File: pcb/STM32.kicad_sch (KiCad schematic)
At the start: 17 parts, among them J2 TC2030, J3 Conn_02x08_Top_Bottom, SW1 SW_Push, SW2 SW_Push, U3 STM32F103C8T6, Y1 8MHz

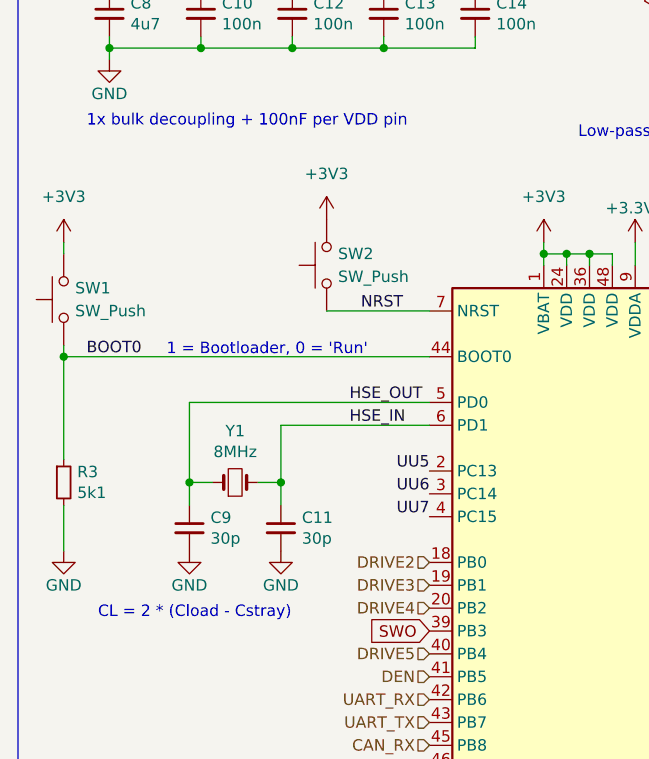
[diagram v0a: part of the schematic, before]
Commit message: Started layout
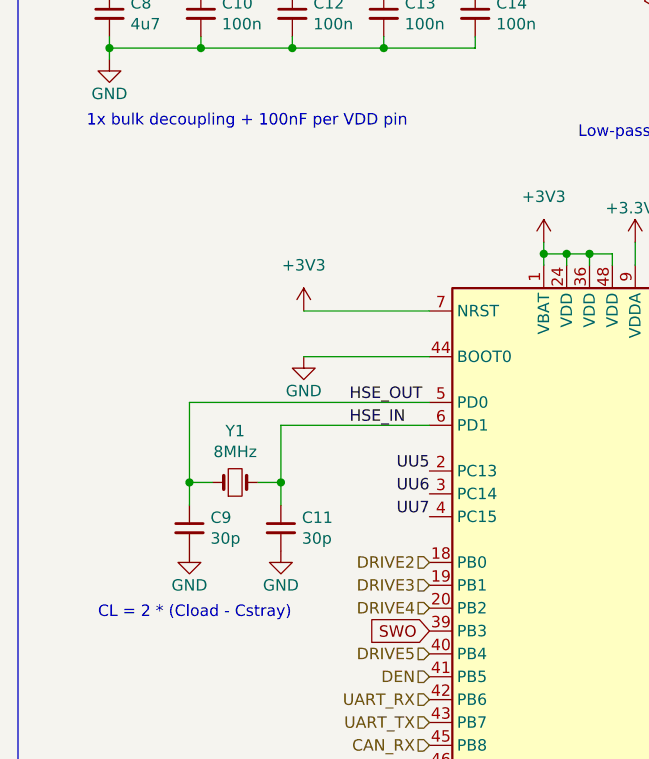
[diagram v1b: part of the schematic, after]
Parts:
- removed R3: 5k1, Resistor_SMD:R_0603_1608Metric, symbol Device:R_Small
- removed SW1, SW2: SW_Push, Button_Switch_SMD:SW_Push_1P1T_NO_CK_KSC7xxJ, symbol Switch:SW_Push
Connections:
- net BOOT0 is gone; now on net GND: U3.44 (BOOT0)
- net NRST is gone; now on net +3V3: U3.7 (NRST)
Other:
- note removed: "1 = Bootloader, 0 = 'Run'"
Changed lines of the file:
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@@
   (junction (at 77.47 52.07) (diameter 0) (color 0 0 0 0)
-  )
-  (junction (at 62.23 93.98) (diameter 0) (color 0 0 0 0)
   )
   (junction (at 87.63 59.69) (diameter 0) (color 0 0 0 0)
@@
     (stroke (width 0) (type default) (color 0 0 0 0))
   )
-  (wire (pts (xy 91.44 88.9) (xy 102.87 88.9))
-    (stroke (width 0) (type default) (color 0 0 0 0))
-  )
   (wire (pts (xy 115.57 162.56) (xy 115.57 161.29))
     (stroke (width 0) (type default) (color 0 0 0 0))
@@
     (stroke (width 0) (type default) (color 0 0 0 0))
   )
-  (wire (pts (xy 102.87 93.98) (xy 62.23 93.98))
-    (stroke (width 0) (type default) (color 0 0 0 0))
-  )
   (wire (pts (xy 134.62 62.23) (xy 134.62 60.96))
     (stroke (width 0) (type default) (color 0 0 0 0))
@@
     (stroke (width 0) (type default) (color 0 0 0 0))
   )
-  (wire (pts (xy 62.23 93.98) (xy 62.23 105.41))
-    (stroke (width 0) (type default) (color 0 0 0 0))
-  )
   (wire (pts (xy 143.51 53.34) (xy 134.62 53.34))
     (stroke (width 0) (type default) (color 0 0 0 0))
@@
     (stroke (width 0) (type default) (color 0 0 0 0))
   )
-  (wire (pts (xy 62.23 81.28) (xy 62.23 82.55))
-    (stroke (width 0) (type default) (color 0 0 0 0))
-  )
   (wire (pts (xy 134.62 59.69) (xy 134.62 60.96))
     (stroke (width 0) (type default) (color 0 0 0 0))
   )
-  (wire (pts (xy 62.23 115.57) (xy 62.23 110.49))
-    (stroke (width 0) (type default) (color 0 0 0 0))
-  )
   (polyline (pts (xy 57.15 170.18) (xy 166.37 170.18))
     (stroke (width 0) (type default) (color 0 0 0 0))
@@
     (stroke (width 0) (type default) (color 0 0 0 0))
   )
+  (wire (pts (xy 88.9 88.9) (xy 102.87 88.9))
+    (stroke (width 0) (type default) (color 0 0 0 0))
+  )
   (wire (pts (xy 86.36 110.49) (xy 86.36 107.95))
     (stroke (width 0) (type default) (color 0 0 0 0))
@@
     (stroke (width 0) (type default) (color 0 0 0 0))
   )
-  (wire (pts (xy 62.23 92.71) (xy 62.23 93.98))
+  (wire (pts (xy 88.9 93.98) (xy 102.87 93.98))
     (stroke (width 0) (type default) (color 0 0 0 0))
   )
@@
     (effects (font (size 2.0066 2.0066) (thickness 0.4013) bold) (justify left bottom))
   )
-  (text "1 = Bootloader, 0 = 'Run'" (at 73.66 93.98 0)
-    (effects (font (size 1.27 1.27)) (justify left bottom))
-  )
   (text "Programming/debug header.\nPlace in an accessible location close to the mcu."
     (at 181.61 105.41 0)
@@
     (effects (font (size 1.27 1.27)) (justify right bottom))
   )
-  (label "NRST" (at 95.25 88.9 0)
-    (effects (font (size 1.27 1.27)) (justify left bottom))
-  )
   (label "UU3" (at 95.25 152.4 180)
     (effects (font (size 1.27 1.27)) (justify right bottom))
@@
   (label "UU2" (at 95.25 149.86 180)
     (effects (font (size 1.27 1.27)) (justify right bottom))
-  )
-  (label "BOOT0" (at 64.77 93.98 0)
-    (effects (font (size 1.27 1.27)) (justify left bottom))
   )
   (label "UU1" (at 193.04 130.81 180)
@@
     (pin "1")
   )
-  (symbol (lib_id "Device:R_Small") (at 62.23 107.95 0) (unit 1)
-    (in_bom yes) (on_board yes)
-    (property "Reference" "R3" (id 0) (at 63.7286 106.7816 0)
-      (effects (font (size 1.27 1.27)) (justify left))
-    )
-    (property "Value" "5k1" (id 1) (at 63.7286 109.093 0)
-      (effects (font (size 1.27 1.27)) (justify left))
-    )
-    (property "Footprint" "Resistor_SMD:R_0603_1608Metric" (id 2) (at 62.23 107.95 0)
-      (effects (font (size 1.27 1.27)) hide)
-    )
-    (property "Datasheet" "~" (id 3) (at 62.23 107.95 0)
-      (effects (font (size 1.27 1.27)) hide)
-    )
-    (property "LCSC" "C25905" (id 5) (at 62.23 107.95 0)
-      (effects (font (size 1.27 1.27)) hide)
-    )
-    (pin "1")
-    (pin "2")
-  )
-  (symbol (lib_id "Switch:SW_Push") (at 62.23 87.63 90) (unit 1)
+  (symbol (lib_id "power:+3V3") (at 88.9 88.9 0) (unit 1)
     (in_bom yes) (on_board yes) (fields_autoplaced)
-    (property "Reference" "SW1" (id 0) (at 63.5 86.3599 90)
-      (effects (font (size 1.27 1.27)) (justify right))
-    )
-    (property "Value" "SW_Push" (id 1) (at 63.5 88.8999 90)
-      (effects (font (size 1.27 1.27)) (justify right))
-    )
-    (property "Footprint" "Button_Switch_SMD:SW_Push_1P1T_NO_CK_KSC7xxJ" (id 2) (at 57.15 87.63 0)
-      (effects (font (size 1.27 1.27)) hide)
-    )
-    (property "Datasheet" "~" (id 3) (at 57.15 87.63 0)
-      (effects (font (size 1.27 1.27)) hide)
-    )
-    (property "LCSC" "C318884" (id 5) (at 62.23 87.63 0)
-      (effects (font (size 1.27 1.27)) hide)
-    )
-    (pin "1")
-    (pin "2")
+    (property "Reference" "#PWR?" (id 0) (at 88.9 92.71 0)
+      (effects (font (size 1.27 1.27)) hide)
+    )
+    (property "Value" "+3V3" (id 1) (at 88.9 83.82 0))
+    (property "Footprint" "" (id 2) (at 88.9 88.9 0)
+      (effects (font (size 1.27 1.27)) hide)
+    )
+    (property "Datasheet" "" (id 3) (at 88.9 88.9 0)
+      (effects (font (size 1.27 1.27)) hide)
+    )
+    (pin "1")
   )
   (symbol (lib_id "MCU_ST_STM32F1:STM32F103C8Tx") (at 120.65 121.92 0) (unit 1)
@@
     (pin "2")
   )
-  (symbol (lib_id "Switch:SW_Push") (at 91.44 83.82 90) (unit 1)
-    (in_bom yes) (on_board yes) (fields_autoplaced)
-    (property "Reference" "SW2" (id 0) (at 92.71 82.5499 90)
-      (effects (font (size 1.27 1.27)) (justify right))
-    )
-    (property "Value" "SW_Push" (id 1) (at 92.71 85.0899 90)
-      (effects (font (size 1.27 1.27)) (justify right))
-    )
-    (property "Footprint" "Button_Switch_SMD:SW_Push_1P1T_NO_CK_KSC7xxJ" (id 2) (at 86.36 83.82 0)
-      (effects (font (size 1.27 1.27)) hide)
-    )
-    (property "Datasheet" "~" (id 3) (at 86.36 83.82 0)
-      (effects (font (size 1.27 1.27)) hide)
-    )
-    (property "LCSC" "C318884" (id 5) (at 91.44 83.82 0)
-      (effects (font (size 1.27 1.27)) hide)
-    )
-    (pin "1")
-    (pin "2")
-  )
   (symbol (lib_id "power:GND") (at 185.42 95.25 0) (unit 1)
     (in_bom yes) (on_board yes)
@@
     (pin "6")
   )
-  (symbol (lib_id "power:+3V3") (at 62.23 81.28 0) (unit 1)
-    (in_bom yes) (on_board yes) (fields_autoplaced)
-    (property "Reference" "#PWR011" (id 0) (at 62.23 85.09 0)
-      (effects (font (size 1.27 1.27)) hide)
-    )
-    (property "Value" "+3V3" (id 1) (at 62.23 76.2 0))
-    (property "Footprint" "" (id 2) (at 62.23 81.28 0)
-      (effects (font (size 1.27 1.27)) hide)
-    )
-    (property "Datasheet" "" (id 3) (at 62.23 81.28 0)
-      (effects (font (size 1.27 1.27)) hide)
-    )
-    (pin "1")
-  )
-  (symbol (lib_id "power:+3V3") (at 91.44 78.74 0) (unit 1)
-    (in_bom yes) (on_board yes) (fields_autoplaced)
-    (property "Reference" "#PWR017" (id 0) (at 91.44 82.55 0)
-      (effects (font (size 1.27 1.27)) hide)
-    )
-    (property "Value" "+3V3" (id 1) (at 91.44 73.66 0))
-    (property "Footprint" "" (id 2) (at 91.44 78.74 0)
-      (effects (font (size 1.27 1.27)) hide)
-    )
-    (property "Datasheet" "" (id 3) (at 91.44 78.74 0)
-      (effects (font (size 1.27 1.27)) hide)
-    )
-    (pin "1")
-  )
   (symbol (lib_id "Device:C_Small") (at 143.51 57.15 0) (unit 1)
     (in_bom yes) (on_board yes)
@@
     (pin "1")
   )
-  (symbol (lib_id "power:GND") (at 62.23 115.57 0) (unit 1)
-    (in_bom yes) (on_board yes)
-    (property "Reference" "#PWR012" (id 0) (at 62.23 121.92 0)
-      (effects (font (size 1.27 1.27)) hide)
-    )
-    (property "Value" "GND" (id 1) (at 62.23 119.38 0))
-    (property "Footprint" "" (id 2) (at 62.23 115.57 0)
-      (effects (font (size 1.27 1.27)) hide)
-    )
-    (property "Datasheet" "" (id 3) (at 62.23 115.57 0)
-      (effects (font (size 1.27 1.27)) hide)
-    )
+  (symbol (lib_id "power:GND") (at 88.9 93.98 0) (unit 1)
+    (in_bom yes) (on_board yes)
+    (property "Reference" "#PWR012" (id 0) (at 88.9 100.33 0)
+      (effects (font (size 1.27 1.27)) hide)
+    )
+    (property "Value" "GND" (id 1) (at 88.9 97.79 0))
+    (property "Footprint" "" (id 2) (at 88.9 93.98 0)
+      (effects (font (size 1.27 1.27)) hide)
+    )
+    (property "Datasheet" "" (id 3) (at 88.9 93.98 0)
+      (effects (font (size 1.27 1.27)) hide)
+    )

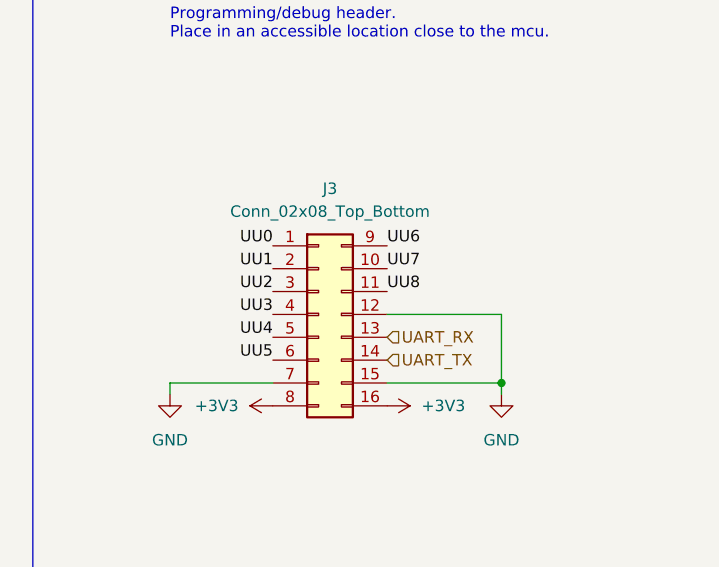
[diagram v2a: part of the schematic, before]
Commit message: Fixed ERC
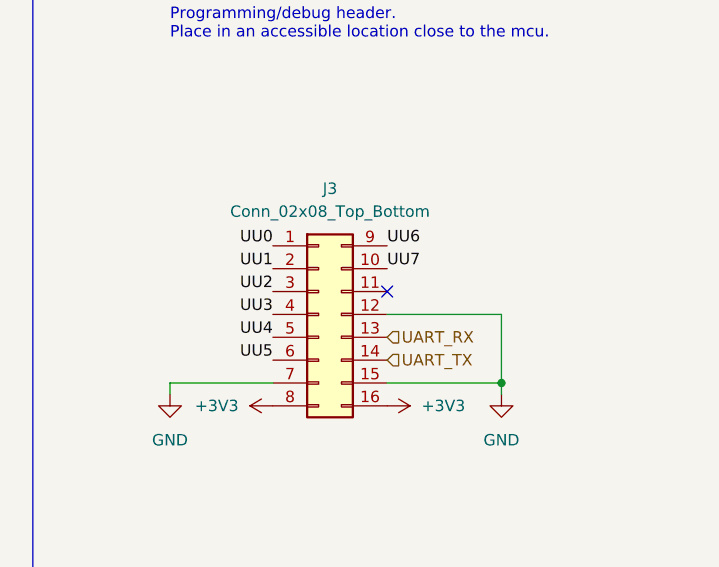
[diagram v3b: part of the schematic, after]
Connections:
- net UU8: no longer names the net of J3.11 (Pin_11)
- no-connect marks 1 -> 2
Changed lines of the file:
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@@
   (junction (at 134.62 60.96) (diameter 0) (color 0 0 0 0)
   )
+  (no_connect (at 205.74 133.35))
   (no_connect (at 186.69 91.44))
   (wire (pts (xy 181.61 144.78) (xy 181.61 143.51))
@@
     (effects (font (size 1.27 1.27)) (justify left bottom))
   )
-  (label "UU8" (at 205.74 133.35 0)
-    (effects (font (size 1.27 1.27)) (justify left bottom))
-  )

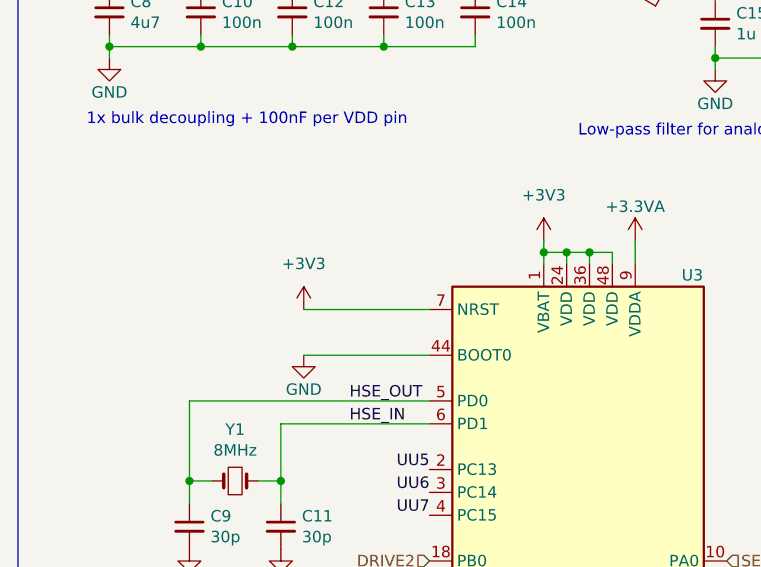
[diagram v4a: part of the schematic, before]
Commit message: Correct PCB to fix firmware flashing (#14)
* Disconnected NRESET

* Udpate date/revision of BCM
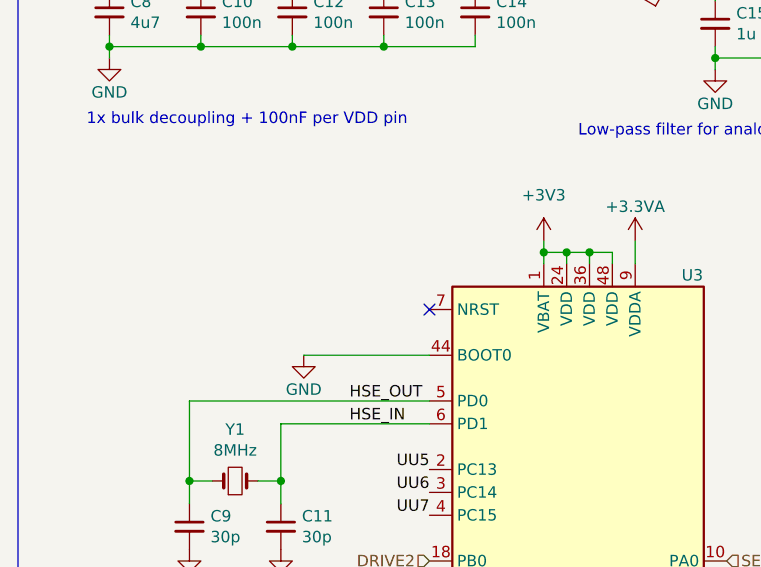
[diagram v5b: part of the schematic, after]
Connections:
- net +3V3: no longer U3.7 (NRST)
- no-connect marks 2 -> 3
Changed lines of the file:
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@@
   (junction (at 134.62 60.96) (diameter 0) (color 0 0 0 0)
   )
+  (no_connect (at 102.87 88.9))
   (no_connect (at 205.74 133.35))
   (no_connect (at 186.69 91.44))
@@
     (stroke (width 0) (type default) (color 0 0 0 0))
   )
-  (wire (pts (xy 88.9 88.9) (xy 102.87 88.9))
-    (stroke (width 0) (type default) (color 0 0 0 0))
-  )
   (wire (pts (xy 86.36 110.49) (xy 86.36 107.95))
     (stroke (width 0) (type default) (color 0 0 0 0))
@@
       (effects (font (size 1.27 1.27)) hide)
     )
-    (pin "1")
-  )
-  (symbol (lib_id "power:+3V3") (at 88.9 88.9 0) (unit 1)
-    (in_bom yes) (on_board yes) (fields_autoplaced)
-    (property "Reference" "#PWR022" (id 0) (at 88.9 92.71 0)
-      (effects (font (size 1.27 1.27)) hide)
-    )
-    (property "Value" "+3V3" (id 1) (at 88.9 83.82 0))
-    (property "Footprint" "" (id 2) (at 88.9 88.9 0)
-      (effects (font (size 1.27 1.27)) hide)
-    )
-    (property "Datasheet" "" (id 3) (at 88.9 88.9 0)
-      (effects (font (size 1.27 1.27)) hide)
-    )
